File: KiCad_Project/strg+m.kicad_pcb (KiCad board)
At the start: 2 copper layers, 60.7 x 128.5 mm, 32 parts, among them J1 Conn_01x04_Female, J10 Conn_01x03_Male, J11 Conn_01x02_Male, J2 Conn_01x03_Female, J3 Conn_01x03_Female, J4 Conn_01x02_Female, J5 AudioJack2, J6 AudioJack2, J7 Conn_02x05_Odd_Even, J8 Conn_01x04_Male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

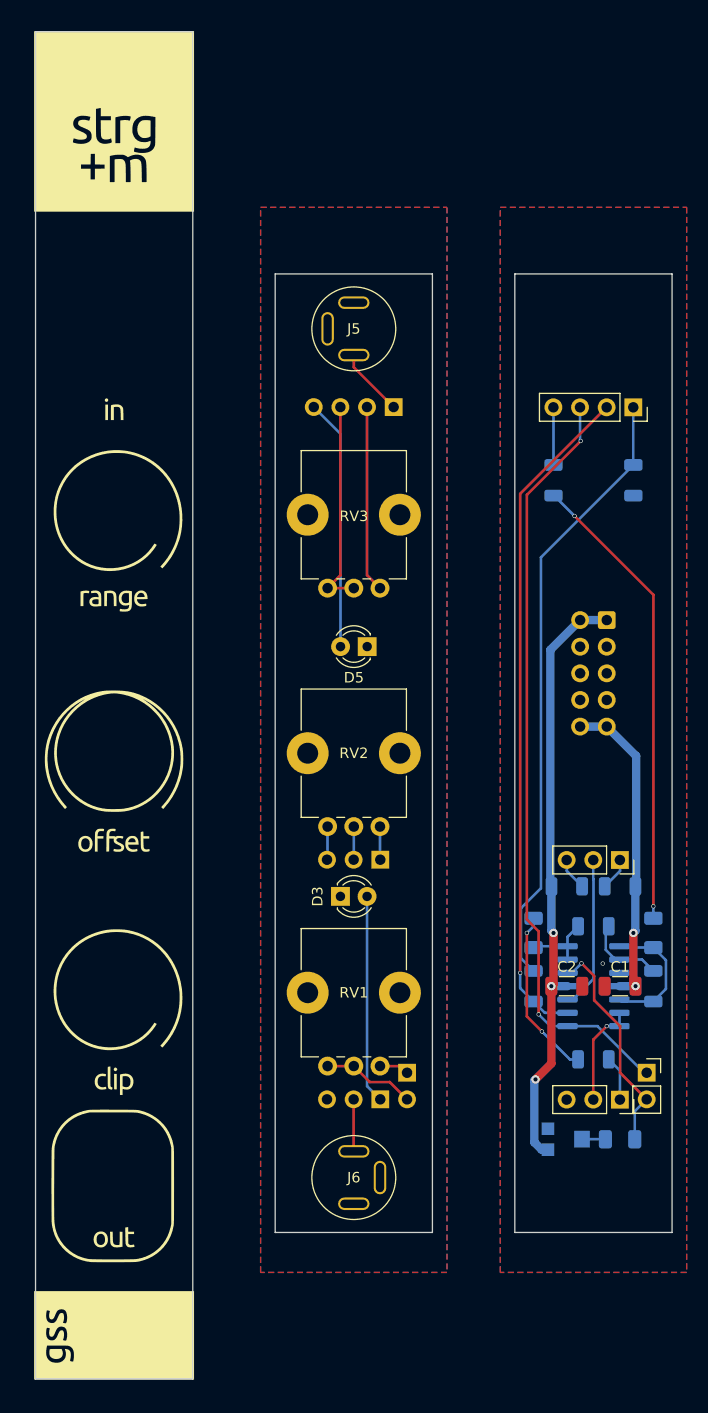
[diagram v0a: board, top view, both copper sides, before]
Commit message: add fronplate to pcb layout
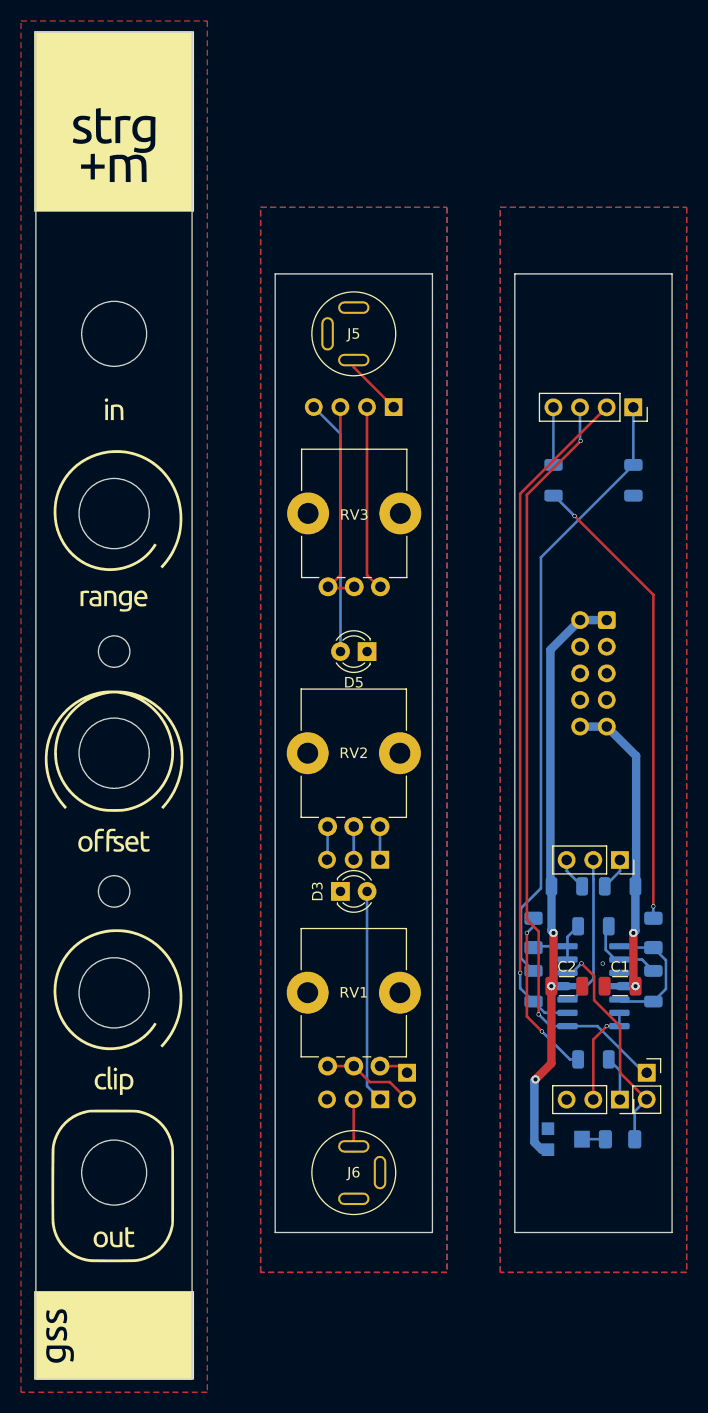
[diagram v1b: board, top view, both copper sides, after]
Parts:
- added REF**: LED_3mm_Drill_Hole_Panel, OS_Drill_Holes:LED_3mm_Drill_Hole_Panel, F.Cu at (-22.9, -45.7)
- added REF**: LED_3mm_Drill_Hole_Panel, OS_Drill_Holes:LED_3mm_Drill_Hole_Panel, F.Cu at (-22.9, -68.6)
- added REF**: RK097_Drill_Hole_Panel, OS_Drill_Holes:RK097_Drill_Hole_Panel, F.Cu at (-22.9, -57.1)
- added REF**: 3HP_Front_Panel, OS_Front_Panels:3HP_Front_Panel, F.Cu at (-30.3, -125.9)
- added REF**: PJ392_Drill_Hole_Panel, OS_Drill_Holes:PJ392_Drill_Hole_Panel, F.Cu at (-22.9, -17.1)
- added REF**: RK097_Drill_Hole_Panel, OS_Drill_Holes:RK097_Drill_Hole_Panel, F.Cu at (-22.9, -34.3)
- added REF**: PJ392_Drill_Hole_Panel, OS_Drill_Holes:PJ392_Drill_Hole_Panel, F.Cu at (-22.9, -97.2)
- added REF**: RK097_Drill_Hole_Panel, OS_Drill_Holes:RK097_Drill_Hole_Panel, F.Cu at (-22.9, -80.0)
- moved D3 0.48 mm to (-1.27, -44.0)
- moved D5 0.48 mm to (1.27, -66.8)
- moved J6 0.47 mm to (0.00, -17.1)
- moved J5 0.47 mm to (0.00, -97.2)
- moved RV3 0.13 mm to (2.54, -73.0)
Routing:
- added copper zone on F.Cu, net (none)
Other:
- board size 60.7 x 128.5 mm -> 37.9 x 91.4 mm
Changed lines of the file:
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@@
       ) (layer "F.SilkS") (width 0) (fill solid))
   )
+  (footprint "OS_Drill_Holes:LED_3mm_Drill_Hole_Panel" (layer "F.Cu")
+    (at -22.86 -45.72)
+    (attr smd)
+    (fp_text reference "REF**" (at 0 -0.5 unlocked) (layer "F.SilkS") hide
+      (effects (font (size 1 1) (thickness 0.15)))
+    )
+    (fp_text value "LED_3mm_Drill_Hole_Panel" (at 0 1 unlocked) (layer "F.Fab")
+      (effects (font (size 1 1) (thickness 0.15)))
+    )
+    (fp_text user "${REFERENCE}" (at 0 2.5 unlocked) (layer "F.Fab")
+      (effects (font (size 1 1) (thickness 0.15)))
+    )
+    (pad "" np_thru_hole circle (at 0 1.755) (size 3 3) (drill 3) (layers *.Mask))
+  )
+  (footprint "OS_Drill_Holes:LED_3mm_Drill_Hole_Panel" (layer "F.Cu")
+    (at -22.86 -68.58)
+    (attr smd)
+    (fp_text reference "REF**" (at 0 -0.5 unlocked) (layer "F.SilkS") hide
+      (effects (font (size 1 1) (thickness 0.15)))
+    )
+    (fp_text value "LED_3mm_Drill_Hole_Panel" (at 0 1 unlocked) (layer "F.Fab")
+      (effects (font (size 1 1) (thickness 0.15)))
+    )
+    (fp_text user "${REFERENCE}" (at 0 2.5 unlocked) (layer "F.Fab")
+      (effects (font (size 1 1) (thickness 0.15)))
+    )
+    (pad "" np_thru_hole circle (at 0 1.735) (size 3 3) (drill 3) (layers *.Mask))
+  )
+  (footprint "OS_Drill_Holes:RK097_Drill_Hole_Panel" (layer "F.Cu")
+    (at -22.86 -57.15)
+    (fp_text reference "REF**" (at -2.54 2.54 unlocked) (layer "F.SilkS") hide
+      (effects (font (size 1 1) (thickness 0.15)))
+    )
+    (fp_text value "RK097_Drill_Hole_Panel" (at 0 1 unlocked) (layer "F.Fab")
+      (effects (font (size 1 1) (thickness 0.15)))
+    )
+    (fp_text user "${REFERENCE}" (at 0 2.5 unlocked) (layer "F.Fab")
+      (effects (font (size 1 1) (thickness 0.15)))
+    )
+    (pad "" np_thru_hole circle (at 0 0) (size 6.7 6.7) (drill 6.7) (layers *.Mask))
+  )
+  (footprint "OS_Front_Panels:3HP_Front_Panel" (layer "F.Cu")
+    (at -30.3276 -125.9332)
+    (fp_text reference "REF**" (at 0 -0.5 unlocked) (layer "F.SilkS") hide
+      (effects (font (size 1 1) (thickness 0.15)))
+    )
+    (fp_text value "3HP_Front_Panel" (at 7.56 129.58 unlocked) (layer "F.Fab")
+      (effects (font (size 1 1) (thickness 0.15)))
+    )
+    (fp_text user "${REFERENCE}" (at 0 2.5 unlocked) (layer "F.Fab") hide
+      (effects (font (size 1 1) (thickness 0.15)))
+    )
+    (fp_rect (start 0 0) (end 14.9 128.5) (layer "Edge.Cuts") (width 0.12) (fill none))
+    (pad "" np_thru_hole oval (at 7.5 125.5) (size 4.8 3.2) (drill oval 4.8 3.2) (layers *.Mask))
+    (pad "" np_thru_hole oval (at 7.5 3) (size 4.8 3.2) (drill oval 4.8 3.2) (layers *.Mask))
+  )
   (footprint "LED_THT:LED_D3.0mm" (layer "F.Cu")
-    (at 1.275 -67.32 180)
+    (at 1.27 -66.845 180)
     (descr "LED, diameter 3.0mm, 2 pins")
     (tags "LED diameter 3.0mm 2 pins")
@@
   )
   (footprint "component-library:PJ-392" (layer "F.Cu")
-    (at 0 -16.67 -90)
+    (at 0 -17.145 -90)
     (property "Sheetfile" "ctrl-m interface.kicad_sch")
     (property "Sheetname" "ctrl+m interface")
@@
     )
   )
+  (footprint "OS_Drill_Holes:PJ392_Drill_Hole_Panel" (layer "F.Cu")
+    (at -22.86 -17.145)
+    (fp_text reference "REF**" (at 0 -4 unlocked) (layer "F.SilkS") hide
+      (effects (font (size 1 1) (thickness 0.15)))
+    )
+    (fp_text value "PJ392_Drill_Hole_Panel" (at 0 4 unlocked) (layer "F.Fab")
+      (effects (font (size 1 1) (thickness 0.15)))
+    )
+    (fp_text user "${REFERENCE}" (at 0 5.5 unlocked) (layer "F.Fab")
+      (effects (font (size 1 1) (thickness 0.15)))
+    )
+    (pad "" np_thru_hole circle (at 0 0) (size 6.2 6.2) (drill 6.2) (layers *.Mask))
+  )
   (footprint "Potentiometer_THT:Potentiometer_Alps_RK09K_Single_Vertical" (layer "F.Cu")
-    (at 2.5 -72.898 90)
+    (at 2.54 -73.025 90)
     (descr "Potentiometer, vertical, Alps RK09K Single, http://www.alps.com/prod/info/E/HTML/Potentiometer/RotaryPotentiometers/RK09K/RK09K_list.html")
     (tags "Potentiometer vertical Alps RK09K Single")
@@
   )
   (footprint "component-library:PJ-392" (layer "F.Cu")
-    (at 0 -97.63 90)
+    (at 0 -97.155 90)
     (property "Sheetfile" "ctrl-m interface.kicad_sch")
     (property "Sheetname" "ctrl+m interface")
@@
     (pad "T" thru_hole oval (at -2.5 0 90) (size 1.2 3) (drill oval 0.8 2.6) (layers *.Cu *.Mask)
       (net 15 "/ctrl+m interface/cv_in") (pintype "passive"))
+  )
+  (footprint "OS_Drill_Holes:RK097_Drill_Hole_Panel" (layer "F.Cu")
+    (at -22.86 -34.29)
+    (fp_text reference "REF**" (at -2.54 2.54 unlocked) (layer "F.SilkS") hide
+      (effects (font (size 1 1) (thickness 0.15)))
+    )
+    (fp_text value "RK097_Drill_Hole_Panel" (at 0 1 unlocked) (layer "F.Fab")
+      (effects (font (size 1 1) (thickness 0.15)))
+    )
+    (fp_text user "${REFERENCE}" (at 0 2.5 unlocked) (layer "F.Fab")
+      (effects (font (size 1 1) (thickness 0.15)))
+    )
+    (pad "" np_thru_hole circle (at 0 0) (size 6.7 6.7) (drill 6.7) (layers *.Mask))
+  )
+  (footprint "OS_Drill_Holes:PJ392_Drill_Hole_Panel" (layer "F.Cu")
+    (at -22.86 -97.155)
+    (fp_text reference "REF**" (at 0 -4 unlocked) (layer "F.SilkS") hide
+      (effects (font (size 1 1) (thickness 0.15)))
+    )
+    (fp_text value "PJ392_Drill_Hole_Panel" (at 0 4 unlocked) (layer "F.Fab")
+      (effects (font (size 1 1) (thickness 0.15)))
+    )
+    (fp_text user "${REFERENCE}" (at 0 5.5 unlocked) (layer "F.Fab")
+      (effects (font (size 1 1) (thickness 0.15)))
+    )
+    (pad "" np_thru_hole circle (at 0 0) (size 6.2 6.2) (drill 6.2) (layers *.Mask))
   )
   (footprint "Capacitor_SMD:C_1206_3216Metric" (layer "F.Cu")
@@
   )
   (footprint "LED_THT:LED_D3.0mm" (layer "F.Cu")
-    (at -1.275 -43.49)
+    (at -1.27 -43.965)
     (descr "LED, diameter 3.0mm, 2 pins")
     (tags "LED diameter 3.0mm 2 pins")
@@
       (rotate (xyz 0 0 0))
     )
+  )
+  (footprint "OS_Drill_Holes:RK097_Drill_Hole_Panel" (layer "F.Cu")
+    (at -22.86 -80.01)
+    (fp_text reference "REF**" (at -2.54 2.54 unlocked) (layer "F.SilkS") hide
+      (effects (font (size 1 1) (thickness 0.15)))
+    )
+    (fp_text value "RK097_Drill_Hole_Panel" (at 0 1 unlocked) (layer "F.Fab")
+      (effects (font (size 1 1) (thickness 0.15)))
+    )
+    (fp_text user "${REFERENCE}" (at 0 2.5 unlocked) (layer "F.Fab")
+      (effects (font (size 1 1) (thickness 0.15)))
+    )
+    (pad "" np_thru_hole circle (at 0 0) (size 6.7 6.7) (drill 6.7) (layers *.Mask))
   )
   (footprint "Connector_PinSocket_2.54mm:PinSocket_1x03_P2.54mm_Vertical" (layer "F.Cu")
@@
     )
   )
-  (gr_rect (start -30.36 -125.96) (end -15.36 2.54) (layer "Edge.Cuts") (width 0.1) (fill none))
   (gr_line (start 30.36 -102.87) (end 15.36 -102.87) (layer "Edge.Cuts") (width 0.1))
   (gr_line (start -7.5 -102.87) (end -7.5 -11.43) (layer "Edge.Cuts") (width 0.1))
@@
   )
   (dimension (type aligned) (layer "User.1")
-    (pts (xy -0.001001 -79.85039) (xy -0.000001 -56.990156))
+    (pts (xy 0 -80.01) (xy 0 -57.15))
     (height 10.159999)
-    (gr_text "22.8602 mm" (at -9.0105 -68.419879 270.0025064) (layer "User.1")
+    (gr_text "22.8600 mm" (at -11.309999 -68.58 90) (layer "User.1")
       (effects (font (size 1 1) (thickness 0.15)))
     )
@@
   )
   (dimension (type aligned) (layer "User.1")
-    (pts (xy 0.000499 -34.130039) (xy 0 -16.509712))
+    (pts (xy 0 -34.29) (xy 0 -17.145))
     (height 10.159999)
-    (gr_text "17.6203 mm" (at -11.309749 -25.320196 89.99838066) (layer "User.1")
+    (gr_text "17.1450 mm" (at -11.309999 -25.7175 90) (layer "User.1")
       (effects (font (size 1 1) (thickness 0.15)))
     )
@@
   )
   (dimension (type aligned) (layer "User.1")
-    (pts (xy -0.000001 -56.990156) (xy -0.005 -43.49))
+    (pts (xy 0 -57.15) (xy 0 -43.965))
     (height 10.159999)
-    (gr_text "13.5002 mm" (at -11.312498 -50.244266 89.97878808) (layer "User.1")
+    (gr_text "13.1850 mm" (at -11.309999 -50.5575 90) (layer "User.1")
       (effects (font (size 1 1) (thickness 0.15)))
     )
@@
   )
   (dimension (type aligned) (layer "User.1")
-    (pts (xy 0 -97.469712) (xy -0.001001 -79.85039))
+    (pts (xy 0 -97.155) (xy 0 -80.01))
     (height 10.159999)
-    (gr_text "17.6193 mm" (at -11.310499 -88.660693 89.99674813) (layer "User.1")
+    (gr_text "17.1450 mm" (at -11.309999 -88.5825 90) (layer "User.1")
       (effects (font (size 1 1) (thickness 0.15)))
     )
@@
   )
   (dimension (type aligned) (layer "User.1")
-    (pts (xy -0.005 -43.49) (xy 0.000499 -34.130039))
+    (pts (xy 0 -43.965) (xy 0.000499 -34.29))
     (height 10.159999)
-    (gr_text "9.3600 mm" (at -9.012248 -38.804727 270.0336553) (layer "User.1")
+    (gr_text "9.6750 mm" (at -9.00975 -39.127035 270.0029492) (layer "User.1")
       (effects (font (size 1 1) (thickness 0.15)))
     )
@@
   (segment (start 25.385 -26.8775) (end 25.385 -24.105) (width 0.25) (layer "B.Cu") (net 31))
   (segment (start 24.3225 -27.94) (end 25.385 -26.8775) (width 0.25) (layer "B.Cu") (net 31))
+  (zone (net 0) (net_name "") (layer "F.Cu") (hatch edge 0.508)
+    (connect_pads (clearance 0))
+    (min_thickness 0.254) (filled_areas_thickness no)
+    (fill yes (thermal_gap 0.508) (thermal_bridge_width 0.508))
+    (polygon
+      (pts
+        (xy -13.97 3.81)
+        (xy -31.75 3.81)
+        (xy -31.75 -127)
+        (xy -13.97 -127)
+      )
+    )
+  )
   (zone (net 1) (net_name "GND") (layers F&B.Cu) (hatch edge 0.508)
     (connect_pads (clearance 0.2))
